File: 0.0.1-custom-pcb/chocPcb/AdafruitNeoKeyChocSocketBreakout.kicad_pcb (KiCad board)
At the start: 2 copper layers, 17.2 x 17.4 mm, 5 parts, among them J1 HC-FPC-0.5-6P-FH20, SW1 MX SOCKET

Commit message: choc rev1 looking good!
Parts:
- added TP1: TestPoint_Pad_2.0x2.0mm, ProjectParts:TestPoint_Pad_2.0x2.0mm, F.Cu at (145.5, 105.0)
- C1: value 1uF -> 100nF; footprint AdafruitNeoKeyChocSocketBreakout:0603-NO -> ProjectParts:C_0402_1005Metric; moved to B.Cu
- LED1: value WS2812B_SK6812E -> WS2812B-2020; footprint AdafruitNeoKeyChocSocketBreakout:NEO3535_REVERSE -> ProjectParts:LED_WS2812B-2020_PLCC4_2.0x2.0mm; moved to B.Cu
- moved J1 5.24 mm to (148.5, 111.8)
- moved C1 4.55 mm to (150.5, 109.7)
- moved LED1 2.55 mm to (148.5, 109.7)
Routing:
- net VDD: track 31.4 -> 7.52 mm, vias 3 -> 1
- net GND: track 27.8 -> 9.76 mm
- net NEO_OUT: track 21.4 -> 3.79 mm, vias 2 -> 1
- net SWITCHA: track 35.0 -> 17.8 mm, vias 2 -> 0
- net SWITCHC: track 21.1 -> 13.0 mm, vias 0 -> 2
- net NEO_IN: track 10.5 -> 5.12 mm, vias 2 -> 1
- removed copper zone on B.Cu, net GND
- removed copper zone on F.Cu, net GND
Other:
- board size 17.2 x 17.4 mm -> 17.5 x 17.1 mm
- board text added: "Choc"
- board text added: "Rev 1"
- board text removed: "Adafruit / FPC"

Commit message: final work before codex review
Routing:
- net VDD: track 7.52 -> 5.89 mm
- net SWITCHC: track 13.0 -> 12.1 mm
- net GND: track 9.76 -> 10.4 mm
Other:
- outline, holes or cut-outs redrawn

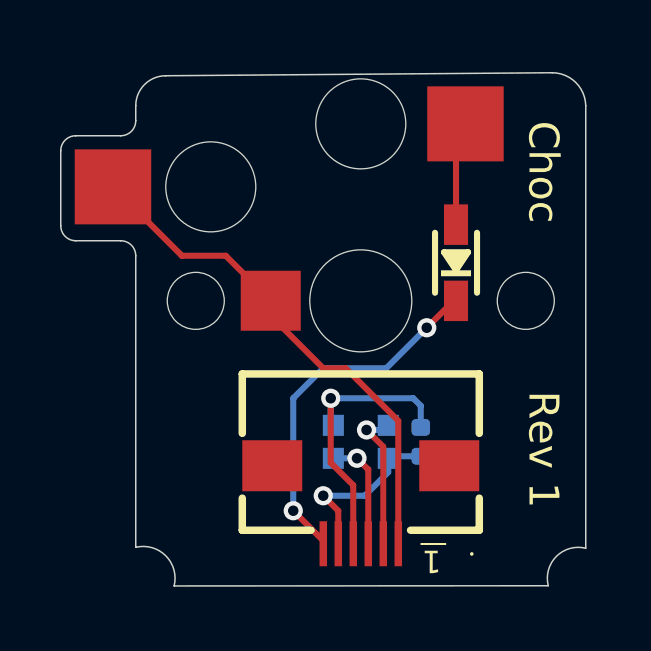
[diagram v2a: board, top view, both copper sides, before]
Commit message: shorten ground line, clean up schematic
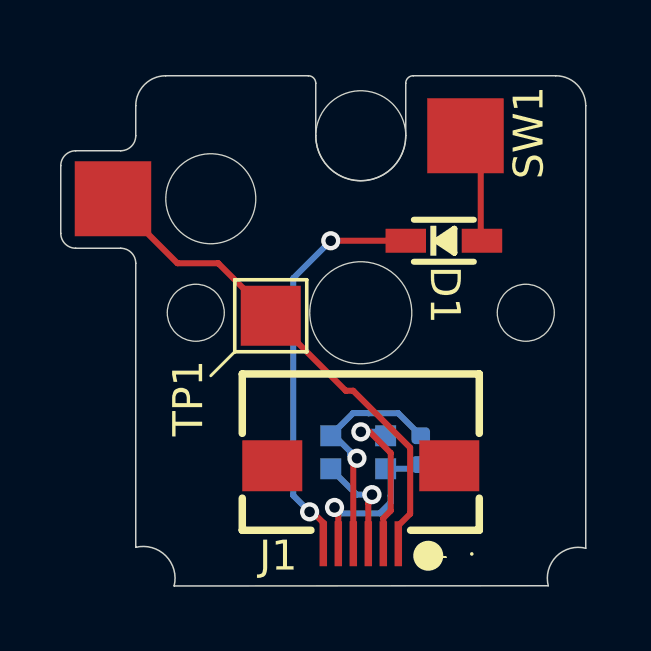
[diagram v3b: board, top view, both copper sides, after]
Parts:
- SW1: value MX SOCKET -> Kailh Choc socket
- moved D1 0.84 mm to (151.3, 103.0), turned to 0 degrees
- moved TP1 0.50 mm to (145.5, 105.5)
- moved SW1 0.40 mm to (148.5, 105.4)
- moved LED1 0.36 mm to (148.4, 110.0)
- moved C1 0.28 mm to (150.5, 110.0)
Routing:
- net GND: track 10.4 -> 7.79 mm
- net SWITCHC: track 12.1 -> 13.6 mm
- net N$2: track 3.56 -> 4.12 mm
- net SWITCHA: track 17.9 -> 18.5 mm
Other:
- board size 17.5 x 17.1 mm -> 17.5 x 17 mm
- board text added: "C1"
- board text added: "chocPcb Rev1"
- board text removed: "Choc"
- board text removed: "Rev 1"

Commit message: make borders square and use dot as pin 1 marker
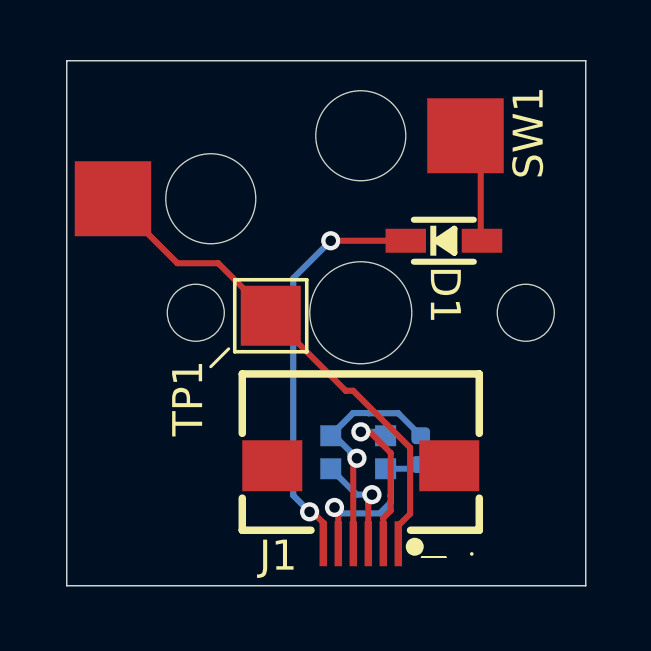
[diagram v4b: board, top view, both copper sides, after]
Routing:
- net SWITCHA: track 18.5 -> 16.7 mm
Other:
- board size 17.5 x 17 mm -> 17.3 x 17.5 mm
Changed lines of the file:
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@@
 	)
 	(gr_line
-		(start 144.3 106.7)
-		(end 143.5 107.5)
+		(start 144.1 106.6)
+		(end 143.5 107.2)
 		(stroke
 			(width 0.1)
@@
 	)
 	(gr_circle
-		(center 150.75 113.5)
-		(end 151.25 113.5)
+		(center 150.3 113.2)
+		(end 150.6 113.2)
 		(stroke
 			(width 0)
@@
 		(layer "B.SilkS")
 	)
-	(gr_arc
-		(start 138.5 100.5)
-		(mid 138.646447 100.146447)
-		(end 139 100)
+	(gr_line
+		(start 138.7 97)
+		(end 156 97)
 		(stroke
 			(width 0.05)
@@
 	)
 	(gr_line
-		(start 138.5 102.75)
-		(end 138.5 100.5)
+		(start 138.7 114.5)
+		(end 138.7 97)
 		(stroke
 			(width 0.05)
@@
 	)
 	(gr_line
-		(start 139 100)
-		(end 140.5 100)
+		(start 156 97)
+		(end 156 114.5)
 		(stroke
 			(width 0.05)
@@
 		(layer "Edge.Cuts")
 	)
-	(gr_arc
-		(start 139 103.25)
-		(mid 138.646447 103.103553)
-		(end 138.5 102.75)
-		(stroke
-			(width 0.05)
-			(type default)
-		)
-		(layer "Edge.Cuts")
-	)
-	(gr_line
-		(start 139 103.25)
-		(end 140.5 103.25)
-		(stroke
-			(width 0.05)
-			(type default)
-		)
-		(layer "Edge.Cuts")
-	)
-	(gr_arc
-		(start 140.5 103.25)
-		(mid 140.853553 103.396447)
-		(end 141 103.75)
-		(stroke
-			(width 0.05)
-			(type default)
-		)
-		(layer "Edge.Cuts")
-	)
-	(gr_arc
-		(start 141 98.500001)
-		(mid 141.292893 97.792893)
-		(end 142.000001 97.5)
-		(stroke
-			(width 0.05)
-			(type default)
-		)
-		(layer "Edge.Cuts")
-	)
-	(gr_arc
-		(start 141 99.500001)
-		(mid 140.853553 99.853554)
-		(end 140.5 100)
-		(stroke
-			(width 0.05)
-			(type default)
-		)
-		(layer "Edge.Cuts")
-	)
-	(gr_line
-		(start 141 99.5)
-		(end 141.000001 98.500001)
-		(stroke
-			(width 0.05)
-			(type default)
-		)
-		(layer "Edge.Cuts")
-	)
-	(gr_line
-		(start 141 113.219224)
-		(end 141 103.75)
-		(stroke
-			(width 0.05)
-			(type default)
-		)
-		(layer "Edge.Cuts")
-	)
-	(gr_arc
-		(start 141 113.219224)
-		(mid 142.002634 113.502644)
-		(end 142.278991 114.507248)
-		(stroke
-			(width 0.05)
-			(type default)
-		)
-		(layer "Edge.Cuts")
-	)
-	(gr_line
-		(start 142.000001 97.5)
-		(end 146.75 97.5)
-		(stroke
-			(width 0.05)
-			(type default)
-		)
-		(layer "Edge.Cuts")
-	)
-	(gr_arc
-		(start 146.75 97.5)
-		(mid 146.926777 97.573223)
-		(end 147 97.75)
-		(stroke
-			(width 0.05)
-			(type default)
-		)
-		(layer "Edge.Cuts")
-	)
-	(gr_line
-		(start 147 97.75)
-		(end 147 99.5)
-		(stroke
-			(width 0.05)
-			(type default)
-		)
-		(layer "Edge.Cuts")
-	)
-	(gr_arc
-		(start 150 97.75)
-		(mid 150.073223 97.573223)
-		(end 150.25 97.5)
-		(stroke
-			(width 0.05)
-			(type default)
-		)
-		(layer "Edge.Cuts")
-	)
-	(gr_arc
-		(start 150 99.5)
-		(mid 148.5 101)
-		(end 147 99.5)
-		(stroke
-			(width 0.05)
-			(type default)
-		)
-		(layer "Edge.Cuts")
-	)
-	(gr_line
-		(start 150 99.5)
-		(end 150 97.75)
-		(stroke
-			(width 0.05)
-			(type default)
-		)
-		(layer "Edge.Cuts")
-	)
-	(gr_line
-		(start 150.25 97.5)
-		(end 155 97.5)
-		(stroke
-			(width 0.05)
-			(type default)
-		)
-		(layer "Edge.Cuts")
-	)
-	(gr_arc
-		(start 154.75 114.499998)
-		(mid 155.021132 113.521131)
-		(end 156 113.25)
-		(stroke
-			(width 0.05)
-			(type default)
-		)
-		(layer "Edge.Cuts")
-	)
-	(gr_line
-		(start 154.750038 114.500143)
-		(end 142.27899 114.507248)
-		(stroke
-			(width 0.05)
-			(type default)
-		)
-		(layer "Edge.Cuts")
-	)
-	(gr_arc
-		(start 155 97.5)
-		(mid 155.707107 97.792893)
-		(end 156 98.5)
-		(stroke
-			(width 0.05)
-			(type default)
-		)
-		(layer "Edge.Cuts")
-	)
-	(gr_line
-		(start 156 98.5)
-		(end 156 113.250002)
+	(gr_line
+		(start 156 114.5)
+		(end 138.7 114.5)
 		(stroke
 			(width 0.05)
@@
 	)
 	(segment
+		(start 145.5 105.5)
+		(end 143.75 103.75)
+		(width 0.2032)
+		(layer "F.Cu")
+		(net 3)
+	)
+	(segment
 		(start 148 108)
 		(end 145.5 105.5)
@@
 	)
 	(segment
+		(start 142.3911 103.75)
+		(end 140.2411 101.6)
+		(width 0.2032)
+		(layer "F.Cu")
+		(net 3)
+	)
+	(segment
+		(start 149.7511 112.4989)
+		(end 150.1463 112.1037)
+		(width 0.2032)
+		(layer "F.Cu")
+		(net 3)
+	)
+	(segment
 		(start 143.75 103.75)
 		(end 142.3911 103.75)
@@
 	)
 	(segment
-		(start 149.7511 112.4989)
-		(end 150.1463 112.1037)
-		(width 0.2032)
-		(layer "F.Cu")
-		(net 3)
-	)
-	(segment
-		(start 140.25 101.2)
-		(end 140.45 101.4)
-		(width 0.2032)
-		(layer "F.Cu")
-		(net 3)
-	)
-	(segment
-		(start 142.3911 103.75)
-		(end 139.8447 101.2036)
-		(width 0.2032)
-		(layer "F.Cu")
-		(net 3)
-	)
-	(segment
-		(start 145.5 105.5)
-		(end 143.75 103.75)
-		(width 0.2032)
-		(layer "F.Cu")
-		(net 3)
-	)
-	(segment
 		(start 150.1463 109.8963)
 		(end 148.25 108)
@@
 	)
 	(segment
-		(start 140.45 101.4)
-		(end 140.95 101.4)
-		(width 0.2032)
-		(layer "F.Cu")
-		(net 3)
-	)
-	(segment
 		(start 149.7511 113.1)
 		(end 149.7511 112.4989)
@@
 		(width 0.2032)
 		(layer "F.Cu")
-		(net 3)
-	)
-	(segment
-		(start 139.8447 101.2036)
-		(end 140.25 101.2)
-		(width 0.2032)
-		(layer "F.Cu")

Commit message: final changes to columnBreakout
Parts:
- D1: value 1N4148 -> 1N4148WS
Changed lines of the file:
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@@
 			)
 		)
-		(property "Value" "1N4148"
+		(property "Value" "1N4148WS"
 			(at 1.5735 0.7415 270)
 			(unlocked yes)
